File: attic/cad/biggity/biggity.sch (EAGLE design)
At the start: 9 parts

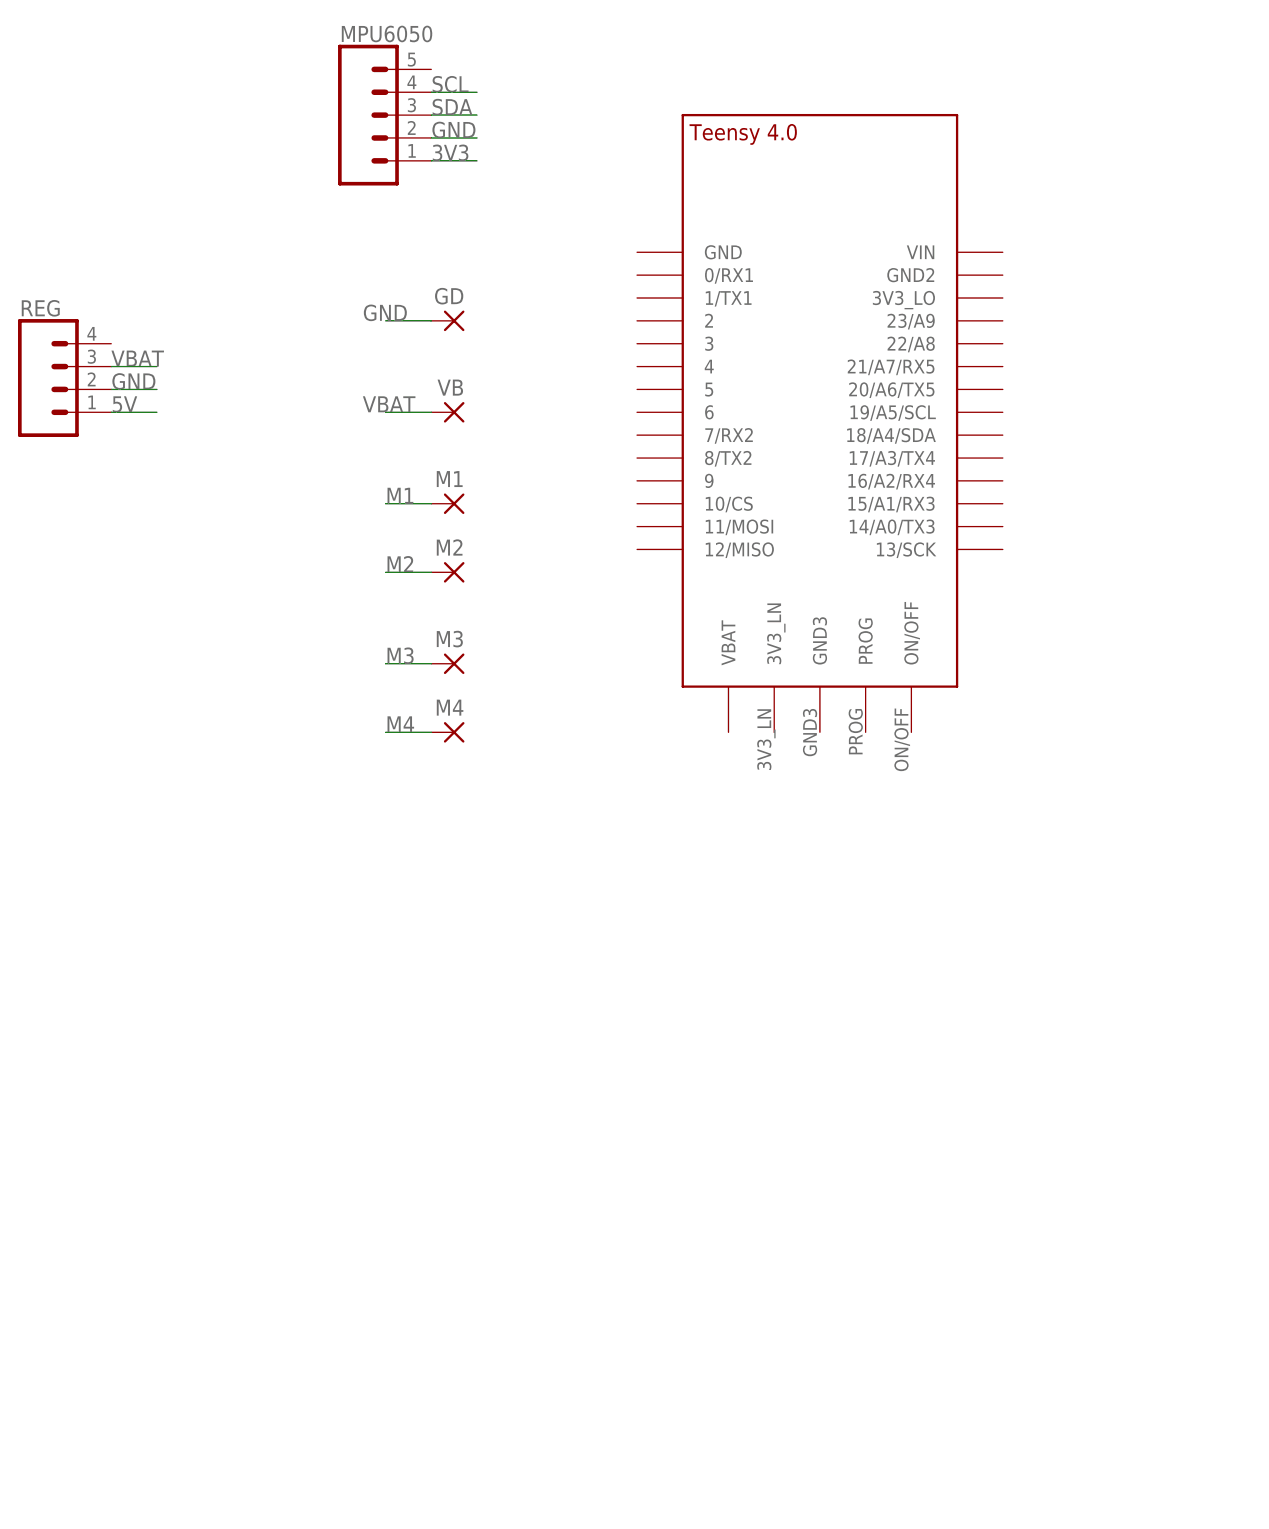
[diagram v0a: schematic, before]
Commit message: new file:   cad/fc.brd
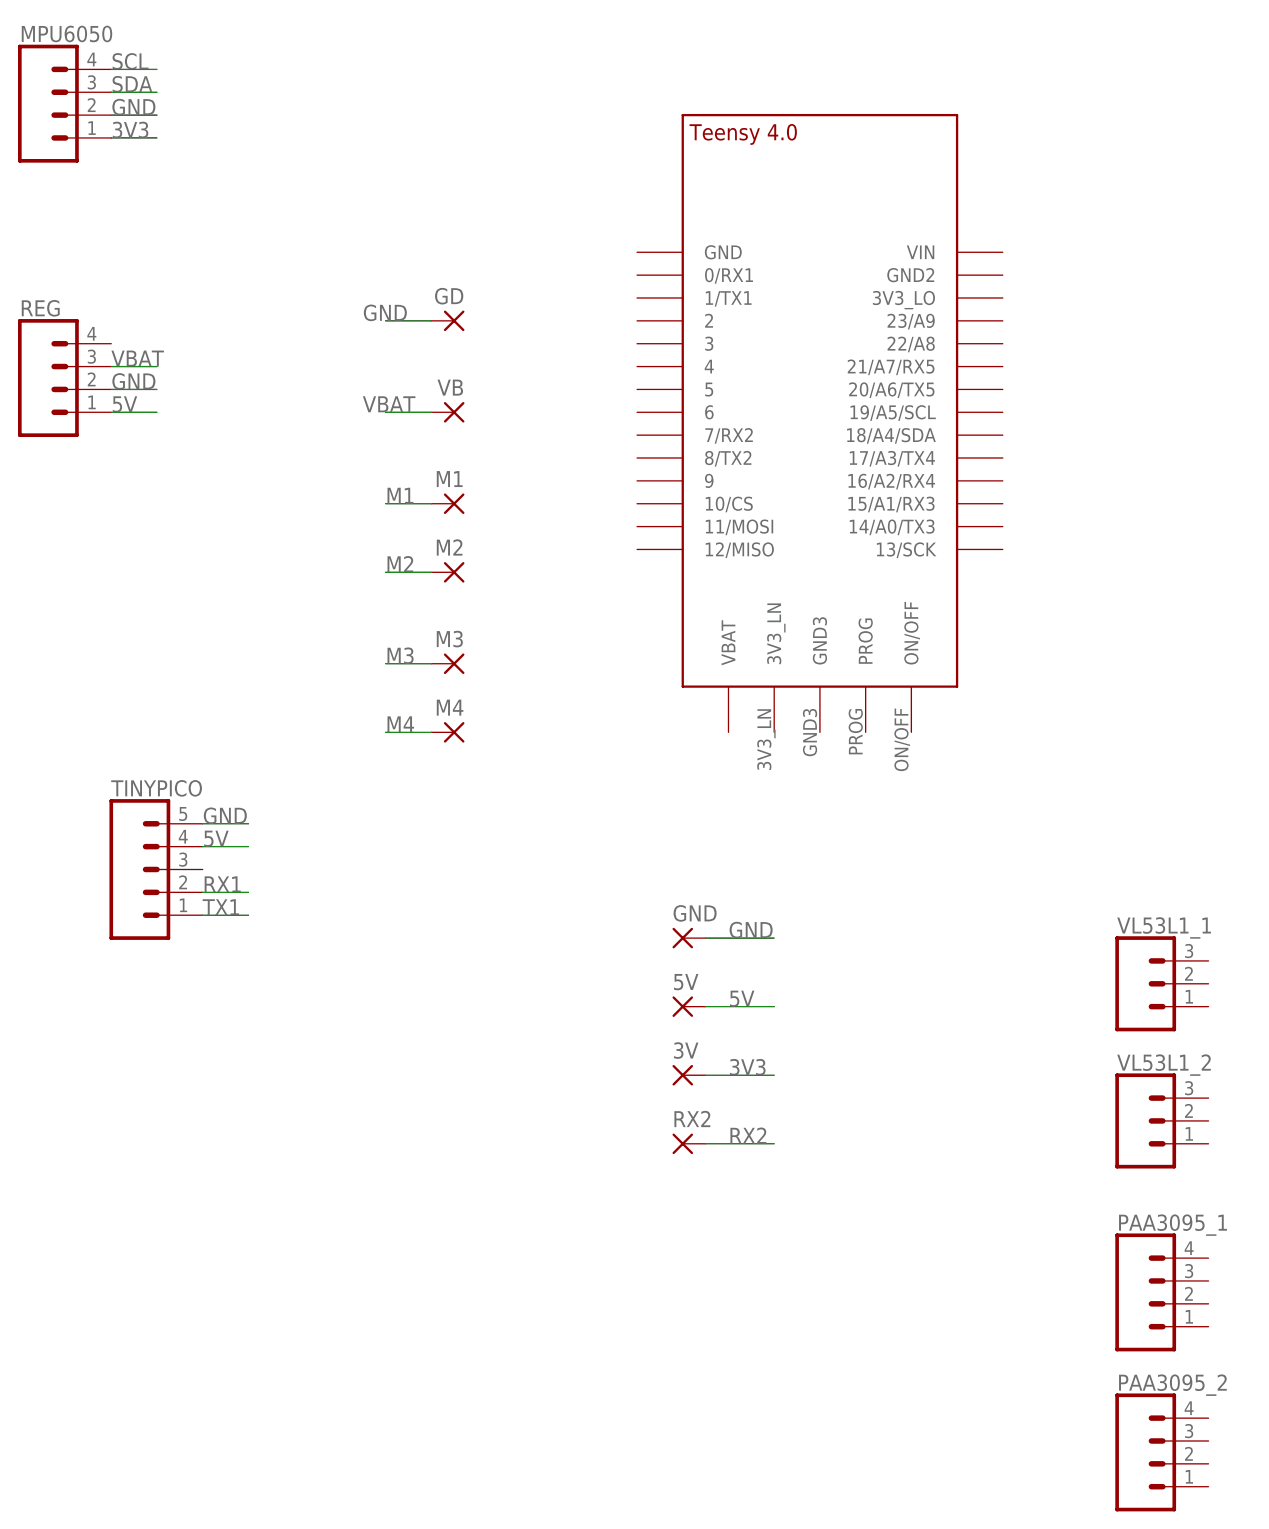
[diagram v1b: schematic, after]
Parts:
- added 3V, 5V, GND, RX2: (no value), wirepad:SMD2
- added PAA3095_1, PAA3095_2: (no value), SparkFun-Connectors:CONN_041X04_NO_SILK
- added TINYPICO: (no value), SparkFun-Connectors:CONN_05NO_SILK
- added VL53L1_1, VL53L1_2: (no value), SparkFun-Connectors:CONN_031X03_NO_SILK
- MPU6050: device SparkFun-Connectors:CONN_05NO_SILK -> SparkFun-Connectors:CONN_041X04_NO_SILK
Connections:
- new net RX1: TINYPICO.2
- new net RX2: RX2.P
- new net TX1: TINYPICO.1
- net 3V3: now also 3V.P
- net 5V: now also 5V.P, TINYPICO.4
- net GND: now also GND.P, TINYPICO.5
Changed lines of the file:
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@@
 </classes>
 <parts>
-<part name="MPU6050" library="SparkFun-Connectors" deviceset="CONN_05" device="NO_SILK"/>
 <part name="REG" library="SparkFun-Connectors" deviceset="CONN_04" device="1X04_NO_SILK"/>
 <part name="GD" library="wirepad" deviceset="SMD2" device=""/>
@@
 <part name="M4" library="wirepad" deviceset="SMD2" device=""/>
 <part name="U$1" library="TEENSY 4.0" deviceset="TEENSY_4.0" device=""/>
+<part name="TINYPICO" library="SparkFun-Connectors" deviceset="CONN_05" device="NO_SILK"/>
+<part name="GND" library="wirepad" deviceset="SMD2" device=""/>
+<part name="5V" library="wirepad" deviceset="SMD2" device=""/>
+<part name="3V" library="wirepad" deviceset="SMD2" device=""/>
+<part name="RX2" library="wirepad" deviceset="SMD2" device=""/>
+<part name="VL53L1_1" library="SparkFun-Connectors" deviceset="CONN_03" device="1X03_NO_SILK"/>
+<part name="VL53L1_2" library="SparkFun-Connectors" deviceset="CONN_03" device="1X03_NO_SILK"/>
+<part name="PAA3095_1" library="SparkFun-Connectors" deviceset="CONN_04" device="1X04_NO_SILK"/>
+<part name="PAA3095_2" library="SparkFun-Connectors" deviceset="CONN_04" device="1X04_NO_SILK"/>
+<part name="MPU6050" library="SparkFun-Connectors" deviceset="CONN_04" device="1X04_NO_SILK"/>
 </parts>
 <sheets>
@@
 </plain>
 <instances>
-<instance part="MPU6050" gate="G$1" x="12.7" y="-25.4" smashed="yes">
-<attribute name="VALUE" x="10.16" y="-35.306" size="1.778" layer="96" font="vector"/>
-<attribute name="NAME" x="10.16" y="-17.272" size="1.778" layer="95" font="vector"/>
-</instance>
 <instance part="REG" gate="J1" x="-20.32" y="-55.88"/>
 <instance part="GD" gate="1" x="22.86" y="-48.26" rot="MR0"/>
@@
 <instance part="M4" gate="1" x="22.86" y="-93.98" rot="MR0"/>
 <instance part="U$1" gate="G$1" x="63.5" y="-53.34"/>
+<instance part="TINYPICO" gate="G$1" x="-12.7" y="-109.22"/>
+<instance part="GND" gate="1" x="48.26" y="-116.84"/>
+<instance part="5V" gate="1" x="48.26" y="-124.46"/>
+<instance part="3V" gate="1" x="48.26" y="-132.08"/>
+<instance part="RX2" gate="1" x="48.26" y="-139.7"/>
+<instance part="VL53L1_1" gate="J$1" x="99.06" y="-121.92"/>
+<instance part="VL53L1_2" gate="J$1" x="99.06" y="-137.16"/>
+<instance part="PAA3095_1" gate="J1" x="101.6" y="-157.48"/>
+<instance part="PAA3095_2" gate="J1" x="101.6" y="-175.26"/>
+<instance part="MPU6050" gate="J1" x="-20.32" y="-25.4"/>
 </instances>
 <busses>
@@
 <net name="3V3" class="0">
 <segment>
-<pinref part="MPU6050" gate="G$1" pin="1"/>
-<wire x1="20.32" y1="-30.48" x2="25.4" y2="-30.48" width="0.1524" layer="91"/>
-<label x="20.32" y="-30.48" size="1.778" layer="95"/>
+<pinref part="3V" gate="1" pin="P"/>
+<wire x1="50.8" y1="-132.08" x2="58.42" y2="-132.08" width="0.1524" layer="91"/>
+<label x="53.34" y="-132.08" size="1.778" layer="95"/>
+</segment>
+<segment>
+<pinref part="MPU6050" gate="J1" pin="1"/>
+<wire x1="-15.24" y1="-27.94" x2="-10.16" y2="-27.94" width="0.1524" layer="91"/>
+<label x="-15.24" y="-27.94" size="1.778" layer="95"/>
 </segment>
 </net>
@@
 </segment>
 <segment>
-<pinref part="MPU6050" gate="G$1" pin="2"/>
-<wire x1="20.32" y1="-27.94" x2="25.4" y2="-27.94" width="0.1524" layer="91"/>
-<label x="20.32" y="-27.94" size="1.778" layer="95"/>
+<pinref part="TINYPICO" gate="G$1" pin="5"/>
+<wire x1="-5.08" y1="-104.14" x2="0" y2="-104.14" width="0.1524" layer="91"/>
+<label x="-5.08" y="-104.14" size="1.778" layer="95"/>
+</segment>
+<segment>
+<pinref part="GND" gate="1" pin="P"/>
+<wire x1="50.8" y1="-116.84" x2="58.42" y2="-116.84" width="0.1524" layer="91"/>
+<label x="53.34" y="-116.84" size="1.778" layer="95"/>
+</segment>
+<segment>
+<pinref part="MPU6050" gate="J1" pin="2"/>
+<wire x1="-15.24" y1="-25.4" x2="-10.16" y2="-25.4" width="0.1524" layer="91"/>
+<label x="-15.24" y="-25.4" size="1.778" layer="95"/>
 </segment>
 </net>
 <net name="SDA" class="0">
 <segment>
-<pinref part="MPU6050" gate="G$1" pin="3"/>
-<wire x1="20.32" y1="-25.4" x2="25.4" y2="-25.4" width="0.1524" layer="91"/>
-<label x="20.32" y="-25.4" size="1.778" layer="95"/>
+<pinref part="MPU6050" gate="J1" pin="3"/>
+<wire x1="-15.24" y1="-22.86" x2="-10.16" y2="-22.86" width="0.1524" layer="91"/>
+<label x="-15.24" y="-22.86" size="1.778" layer="95"/>
 </segment>
 </net>
 <net name="SCL" class="0">
 <segment>
-<pinref part="MPU6050" gate="G$1" pin="4"/>
-<wire x1="20.32" y1="-22.86" x2="25.4" y2="-22.86" width="0.1524" layer="91"/>
-<label x="20.32" y="-22.86" size="1.778" layer="95"/>
+<pinref part="MPU6050" gate="J1" pin="4"/>
+<wire x1="-15.24" y1="-20.32" x2="-10.16" y2="-20.32" width="0.1524" layer="91"/>
+<label x="-15.24" y="-20.32" size="1.778" layer="95"/>
 </segment>
 </net>
@@
 <wire x1="-15.24" y1="-58.42" x2="-10.16" y2="-58.42" width="0.1524" layer="91"/>
 <label x="-15.24" y="-58.42" size="1.778" layer="95"/>
+</segment>
+<segment>
+<pinref part="TINYPICO" gate="G$1" pin="4"/>
+<wire x1="-5.08" y1="-106.68" x2="0" y2="-106.68" width="0.1524" layer="91"/>
+<label x="-5.08" y="-106.68" size="1.778" layer="95"/>
+</segment>
+<segment>
+<pinref part="5V" gate="1" pin="P"/>
+<wire x1="50.8" y1="-124.46" x2="58.42" y2="-124.46" width="0.1524" layer="91"/>
+<label x="53.34" y="-124.46" size="1.778" layer="95"/>
 </segment>
 </net>
@@
 </segment>
 </net>
+<net name="RX2" class="0">
+<segment>
+<pinref part="RX2" gate="1" pin="P"/>
+<wire x1="50.8" y1="-139.7" x2="58.42" y2="-139.7" width="0.1524" layer="91"/>
+<label x="53.34" y="-139.7" size="1.778" layer="95"/>
+</segment>
+</net>
+<net name="RX1" class="0">
+<segment>
+<pinref part="TINYPICO" gate="G$1" pin="2"/>
+<wire x1="-5.08" y1="-111.76" x2="0" y2="-111.76" width="0.1524" layer="91"/>
+<label x="-5.08" y="-111.76" size="1.778" layer="95"/>
+</segment>
+</net>
+<net name="TX1" class="0">
+<segment>
+<pinref part="TINYPICO" gate="G$1" pin="1"/>
+<wire x1="-5.08" y1="-114.3" x2="0" y2="-114.3" width="0.1524" layer="91"/>
+<label x="-5.08" y="-114.3" size="1.778" layer="95"/>
+</segment>
+</net>
